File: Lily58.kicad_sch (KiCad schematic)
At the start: 12 parts, among them J1 USB_C_Receptacle, U1 ESP32-S3-WROOM-2, U3 BQ24090DGQ, U4 AP63203WU, Y1 Crystal_GND24

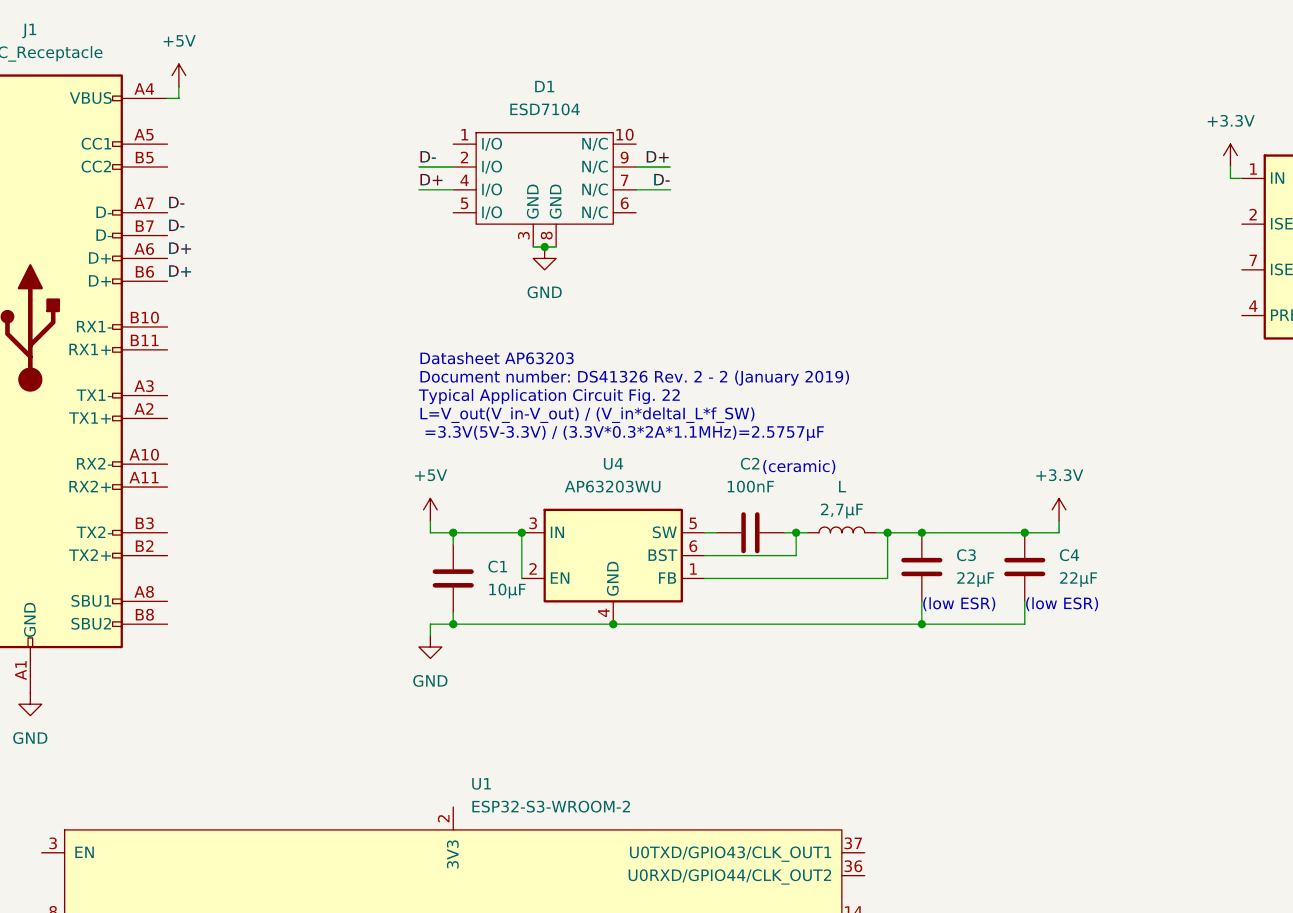
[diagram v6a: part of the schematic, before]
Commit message: USB-C recaptacle connected; cleaner positioning
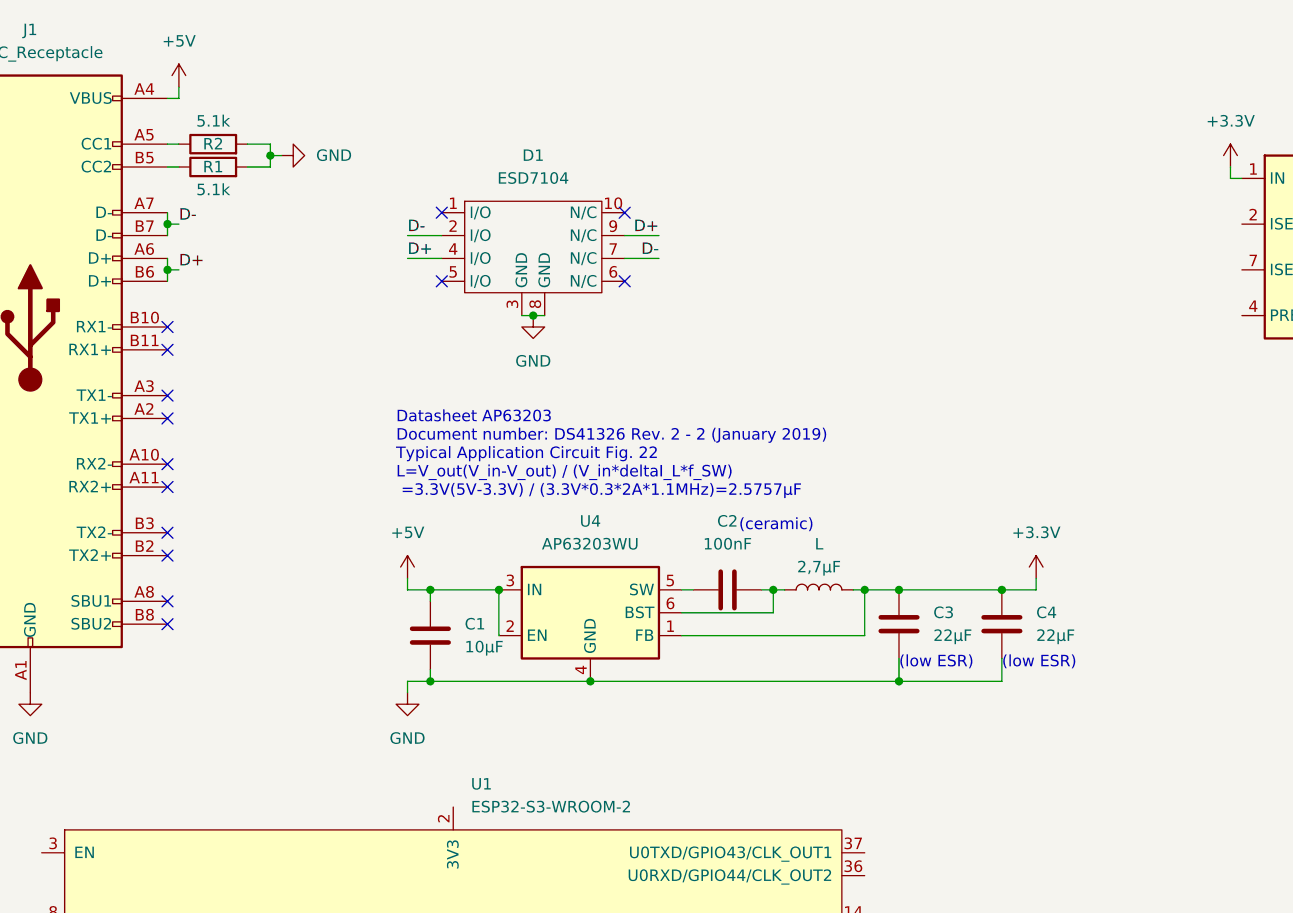
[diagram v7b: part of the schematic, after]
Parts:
- added R1, R2: 5.1k, Resistor_SMD:R_0805_2012Metric_Pad1.20x1.40mm_HandSolder, symbol Device:R
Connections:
- net GND: now also R1.2, R2.2
- net at J1.A5 (CC1): now also R2.1
- net at J1.B5 (CC2): now also R1.1
- no-connect marks 0 -> 14
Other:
- moved on the sheet: C1, C2, C3, C4, D1, L, U4

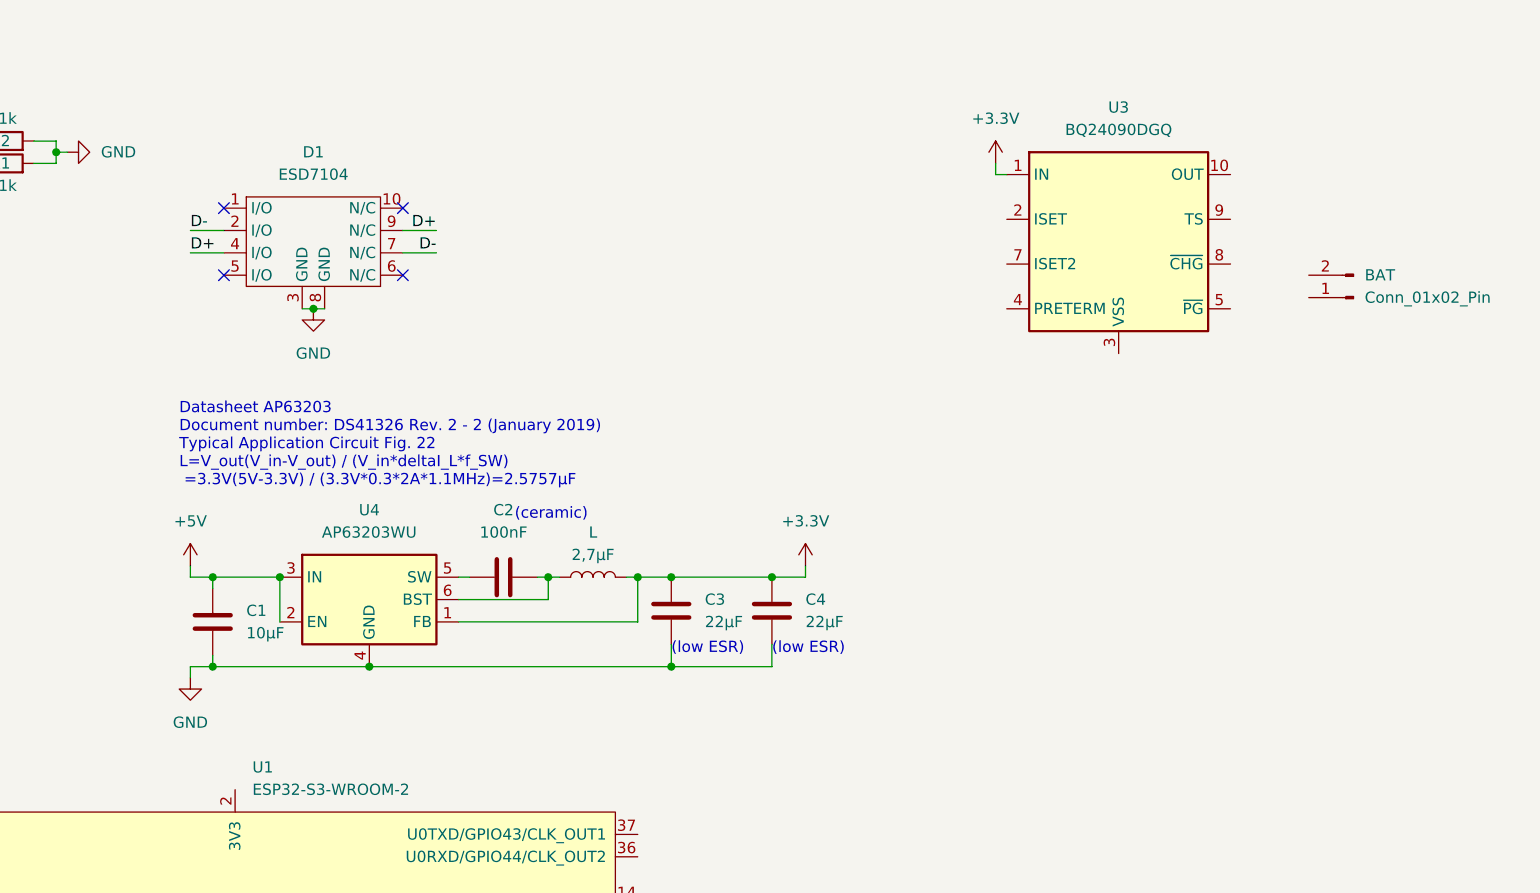
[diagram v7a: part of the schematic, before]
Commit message: swaped order of BQ24090DGQ and AP63203WU
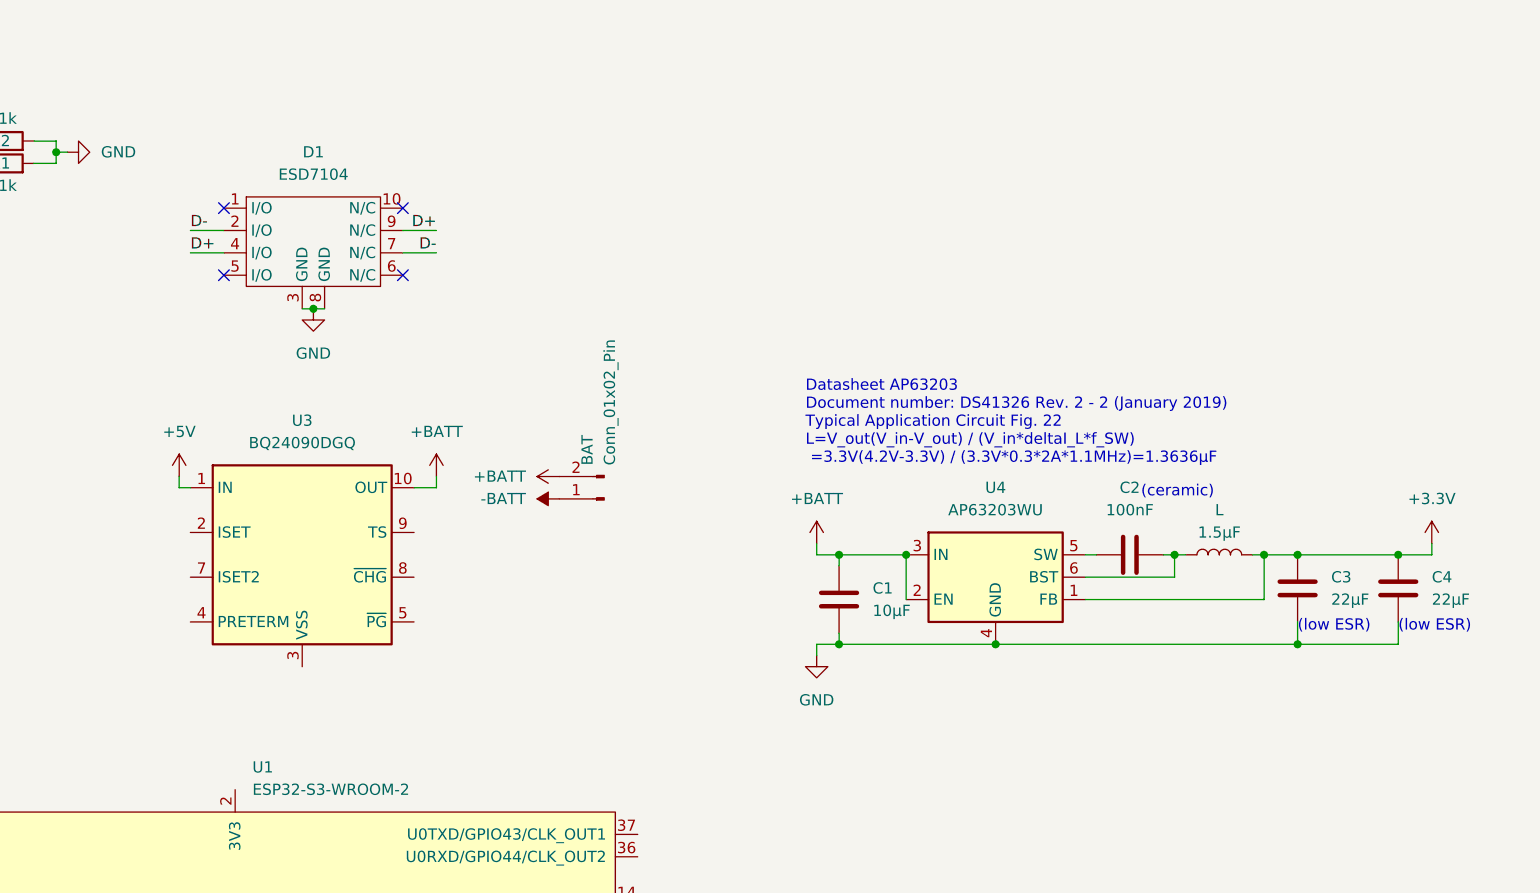
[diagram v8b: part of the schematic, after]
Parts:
- L: value 2,7µF -> 1.5µF
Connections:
- net +3.3V: no longer U3.1 (IN)
- net +5V: now also U3.1 (IN); no longer C1.1, U4.2 (EN), U4.3 (IN)
- net -BATT: now reaches BAT.1 (Pin_1)
- net +BATT: now reaches BAT.2 (Pin_2)
- net +BATT: now also C1.1, U3.10 (OUT), U4.2 (EN), U4.3 (IN)
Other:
- note added: "Datasheet AP63203 Document number: DS41326 Rev. 2 - 2 (January 2019) Typical Application Circuit Fig. 22 L=V_out(V_in-V_out) / (V_in*deltaI_L*f_SW) =3.3V(4.2V-3.3V) / (3.3V*0.3*2A*1.1MHz)=1.3636µF"
- note removed: "Datasheet AP63203 Document number: DS41326 Rev. 2 - 2 (January 2019) Typical Application Circuit Fig. 22 L=V_out(V_in-V_out) / (V_in*deltaI_L*f_SW) =3.3V(5V-3.3V) / (3.3V*0.3*2A*1.1MHz)=2.5757µF"
- moved on the sheet: BAT, C1, C2, C3, C4, L, U3, U4
